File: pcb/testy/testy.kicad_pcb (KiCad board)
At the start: 2 copper layers, 114.5 x 101.4 mm, 94 parts, among them P1 OLED, P2 ICSP, SW0:0 SW_Push, SW0:1 SW_Push, SW0:2 SW_Push, SW0:3 SW_Push, SW0:4 SW_Push, SW1:0 SW_Push, SW1:1 SW_Push, SW1:2 SW_Push, SW1:3 SW_Push, SW1:4 SW_Push, SW2:0 SW_Push, SW2:1 SW_Push, SW2:2 SW_Push, SW2:3 SW_Push, SW2:4 SW_Push, SW3:0 SW_Push, SW3:1 SW_Push, SW3:2 SW_Push, SW3:3 SW_Push, SW3:4 SW_Push, SW3:5 SW_Push, SW4:1 SW_Push, SW4:2 SW_Push, SW4:3 SW_Push, SW4:4 SW_Push, SW4:5 SW_Push

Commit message: fix: undo some wrong decisions with the LEDs
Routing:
- net VCC: track 85.1 -> 61.1 mm, vias 3 -> 2
- net GND: track 238.3 -> 223.2 mm
- net LED: track 71.8 -> 57.4 mm, vias 3 -> 0
- net Net-(LED1-Pad1): track 9.55 -> 0.00 mm, vias 1 -> 0
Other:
- board text added: "TODO add extra data pin so we can handwire LEDs over the TRRS cable"
- board text added: "TODO don't directly connect the halves on the connector"
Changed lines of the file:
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@@
   (general
     (thickness 1.6)
-    (drawings 1027)
-    (tracks 1410)
+    (drawings 1029)
+    (tracks 1372)
     (zones 0)
     (modules 94)
@@
     (pad 1 thru_hole circle (at 1.166726 -1.166726 270) (size 0.7 0.7) (drill 0.4) (layers *.Cu *.Mask))
   )
+  (gr_text "TODO add extra data pin so we can\nhandwire LEDs over the TRRS cable" (at 201.83 107.7) (layer Dwgs.User)
+    (effects (font (size 1 1) (thickness 0.15)))
+  )
+  (gr_text "TODO don't directly connect the halves on the connector" (at 209.74 103.79) (layer Dwgs.User)
+    (effects (font (size 1 1) (thickness 0.15)))
+  )
   (gr_text "OLED I2C resistors" (at 170.4 90.3 90) (layer F.SilkS)
     (effects (font (size 1 1) (thickness 0.15)))
@@
   (segment (start 181.51 80.97212) (end 182.16106 80.32106) (width 0.25) (layer F.Cu) (net 5))
   (segment (start 181.51 81.53962) (end 181.51 80.97212) (width 0.25) (layer F.Cu) (net 5))
-  (segment (start 184.12 104.99) (end 184.12 98.79) (width 0.25) (layer B.Cu) (net 5))
   (segment (start 184.12 105.99) (end 184.12 104.99) (width 0.25) (layer B.Cu) (net 5))
   (segment (start 179.04 98.79) (end 179.04 97.79) (width 0.25) (layer F.Cu) (net 5))
-  (segment (start 178.79 98.79) (end 179.04 98.79) (width 0.25) (layer F.Cu) (net 5))
-  (segment (start 177.244999 100.335001) (end 178.79 98.79) (width 0.25) (layer F.Cu) (net 5))
-  (segment (start 177.244999 101.238001) (end 177.244999 100.335001) (width 0.25) (layer F.Cu) (net 5))
-  (segment (start 179.04 103.033002) (end 177.244999 101.238001) (width 0.25) (layer F.Cu) (net 5))
-  (segment (start 179.04 105.99) (end 179.04 103.033002) (width 0.25) (layer F.Cu) (net 5))
   (via (at 173.03 61.7) (size 0.8) (drill 0.4) (layers F.Cu B.Cu) (net 5))
   (segment (start 178.480001 53.349999) (end 179.33 52.5) (width 0.25) (layer F.Cu) (net 5))
@@
   (segment (start 178.96 80.97212) (end 178.35394 80.36606) (width 0.25) (layer F.Cu) (net 8))
   (segment (start 178.35394 80.36606) (end 175.45 77.46212) (width 0.25) (layer F.Cu) (net 8))
-  (segment (start 179.04 105.99) (end 179.04 98.79) (width 0.25) (layer B.Cu) (net 8))
-  (via (at 181.4 102.04) (size 0.8) (drill 0.4) (layers F.Cu B.Cu) (net 8))
-  (segment (start 181.4 101.26) (end 181.4 102.04) (width 0.25) (layer F.Cu) (net 8))
-  (segment (start 184.12 98.79) (end 183.87 98.79) (width 0.25) (layer F.Cu) (net 8))
-  (segment (start 183.87 98.79) (end 181.4 101.26) (width 0.25) (layer F.Cu) (net 8))
-  (segment (start 179.29 105.99) (end 179.04 105.99) (width 0.25) (layer B.Cu) (net 8))
-  (segment (start 181.4 103.88) (end 179.29 105.99) (width 0.25) (layer B.Cu) (net 8))
-  (segment (start 181.4 102.04) (end 181.4 103.88) (width 0.25) (layer B.Cu) (net 8))
-  (segment (start 184.12 105.99) (end 184.12 98.79) (width 0.25) (layer F.Cu) (net 8))
   (segment (start 176.55 96.55) (end 176.52 96.55) (width 0.25) (layer B.Cu) (net 8))
   (segment (start 178.79 98.79) (end 176.55 96.55) (width 0.25) (layer B.Cu) (net 8))
@@
   (segment (start 176.52 88.305218) (end 177.946499 86.878719) (width 0.25) (layer F.Cu) (net 8))
   (segment (start 176.52 90.6) (end 176.52 88.305218) (width 0.25) (layer F.Cu) (net 8))
-  (segment (start 175.02 94.8) (end 175.02 92.35) (width 0.25) (layer F.Cu) (net 9))
+  (segment (start 175.02 92.35) (end 175.02 94.8) (width 0.25) (layer B.Cu) (net 9))
   (segment (start 93.17 83.145) (end 93.175 83.15) (width 0.25) (layer F.Cu) (net 10))
   (segment (start 93.175 83.15) (end 108.1 83.15) (width 0.25) (layer F.Cu) (net 10))
@@
   (segment (start 180.84 79.07) (end 180.84 78.504315) (width 0.25) (layer F.Cu) (net 45))
   (segment (start 180.84 78.504315) (end 178.84135 76.505665) (width 0.25) (layer F.Cu) (net 45))
-  (segment (start 180.54 100.83) (end 180.17 100.83) (width 0.25) (layer B.Cu) (net 46))
-  (via (at 180.17 100.83) (size 0.8) (drill 0.4) (layers F.Cu B.Cu) (net 46))
-  (segment (start 181.58 98.79) (end 181.58 99.79) (width 0.25) (layer B.Cu) (net 46))
-  (segment (start 181.58 99.79) (end 180.54 100.83) (width 0.25) (layer B.Cu) (net 46))
-  (segment (start 181.33 105.99) (end 181.58 105.99) (width 0.25) (layer F.Cu) (net 46))
-  (segment (start 180.17 104.83) (end 181.33 105.99) (width 0.25) (layer F.Cu) (net 46))
-  (segment (start 180.17 100.83) (end 180.17 104.83) (width 0.25) (layer F.Cu) (net 46))
-  (via (at 177.97 100.89) (size 0.8) (drill 0.4) (layers F.Cu B.Cu) (net 46))
-  (segment (start 180.17 100.83) (end 178.03 100.83) (width 0.25) (layer F.Cu) (net 46))
-  (segment (start 178.03 100.83) (end 177.97 100.89) (width 0.25) (layer F.Cu) (net 46))
-  (segment (start 177.404315 100.89) (end 175.43 98.915685) (width 0.25) (layer B.Cu) (net 46))
-  (segment (start 177.97 100.89) (end 177.404315 100.89) (width 0.25) (layer B.Cu) (net 46))
-  (via (at 175.43 98.915685) (size 0.8) (drill 0.4) (layers F.Cu B.Cu) (net 46))
   (segment (start 184.403701 52.510299) (end 185.28 51.634) (width 0.25) (layer F.Cu) (net 46))
   (segment (start 184.078699 52.835301) (end 184.403701 52.510299) (width 0.25) (layer F.Cu) (net 46))
@@
   (segment (start 173.89 82.54038) (end 173.9 82.53038) (width 0.25) (layer B.Cu) (net 50))
   (segment (start 173.89 84.88) (end 173.89 82.54038) (width 0.25) (layer B.Cu) (net 50))
-  (via (at 182.58 102.98) (size 0.8) (drill 0.4) (layers F.Cu B.Cu) (net 54))
-  (segment (start 181.58 98.79) (end 181.58 99.79) (width 0.25) (layer F.Cu) (net 54))
-  (segment (start 181.266998 102.98) (end 182.58 102.98) (width 0.25) (layer F.Cu) (net 54))
-  (segment (start 181.58 99.79) (end 180.94999 100.42001) (width 0.25) (layer F.Cu) (net 54))
-  (segment (start 180.94999 100.42001) (end 180.94999 101.417008) (width 0.25) (layer F.Cu) (net 54))
-  (segment (start 180.674999 102.388001) (end 181.266998 102.98) (width 0.25) (layer F.Cu) (net 54))
-  (segment (start 180.674999 101.691999) (end 180.674999 102.388001) (width 0.25) (layer F.Cu) (net 54))
-  (segment (start 180.94999 101.417008) (end 180.674999 101.691999) (width 0.25) (layer F.Cu) (net 54))
-  (segment (start 182.58 104.99) (end 181.58 105.99) (width 0.25) (layer B.Cu) (net 54))
-  (segment (start 182.58 102.98) (end 182.58 104.99) (width 0.25) (layer B.Cu) (net 54))
   (zone (net 0) (net_name "") (layer B.Cu) (hatch edge 0.508)
     (connect_pads (clearance 0.508))

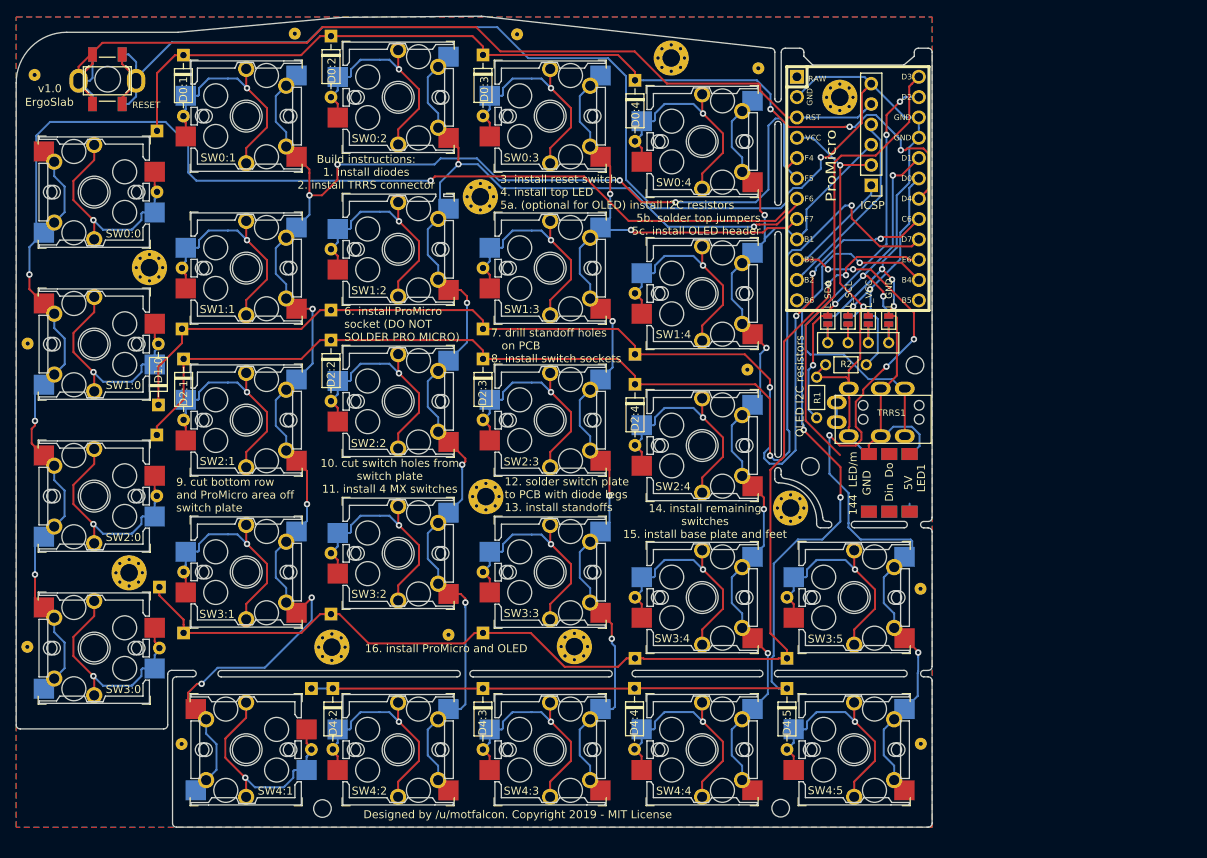
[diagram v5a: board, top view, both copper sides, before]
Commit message: fix: correct (I think) the LED wiring
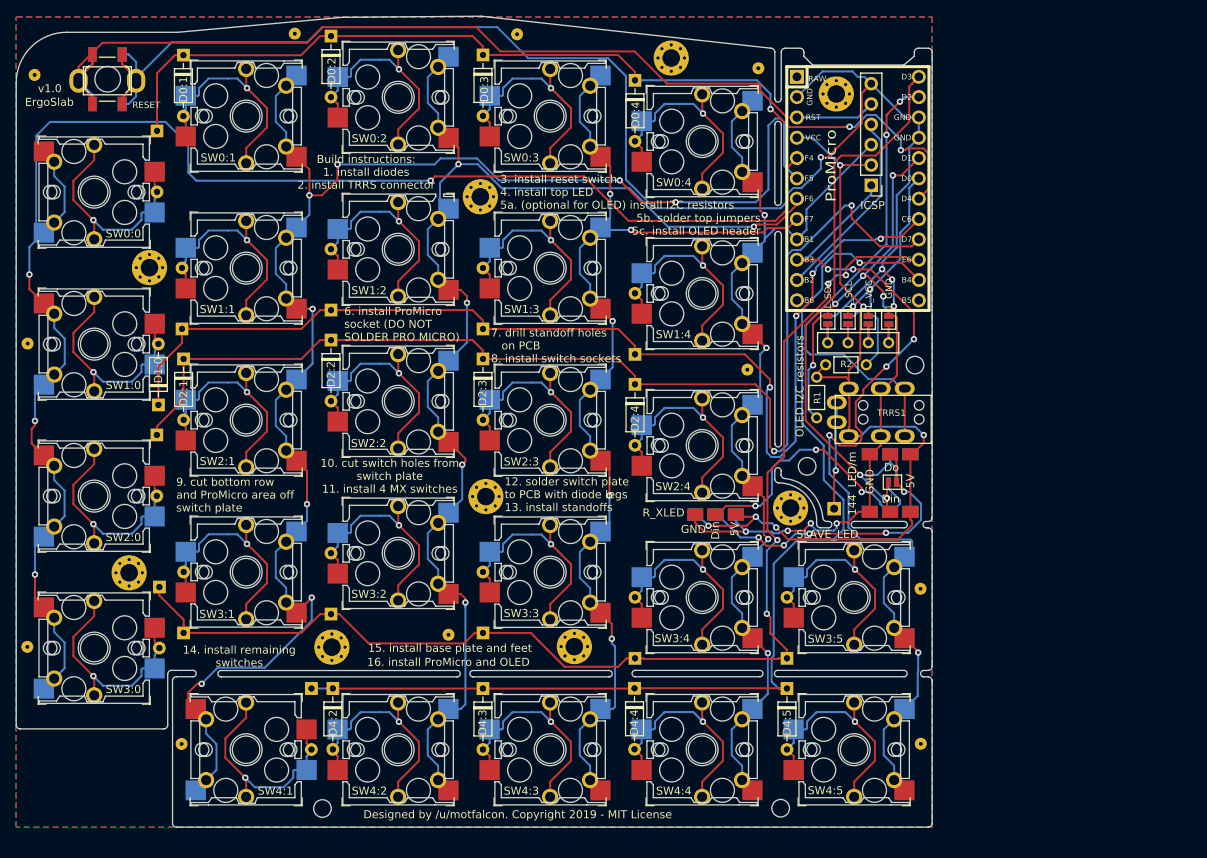
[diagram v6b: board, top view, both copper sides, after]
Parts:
- removed LED1: SK6812mini, footprints:ws2812-single
- added J1: L_XLED, footprints:ws2812-strip, B.Cu at (160.1, 106.0)
- added J2: R_XLED, footprints:ws2812-strip, F.Cu at (159.7, 106.0)
- added J3: SLAVE_LED, footprints:PinHeader_1x01_P2.54mm_Vertical, F.Cu at (174.7, 105.6)
- added JP12: R_NOLED, footprints:Jumper, B.Cu at (182.0, 102.3)
- added JP9: L_NOLED, footprints:Jumper, F.Cu at (182.0, 102.3)
- added LED_L1: SK6812mini, footprints:ws2812-single, F.Cu at (181.5, 102.2)
- added LED_R1: SK6812mini, footprints:ws2812-single, B.Cu at (181.5, 102.6)
- moved Drill 0.61 mm to (175.0, 53.8)
- moved HOLE_M2 0.40 mm to (171.3, 100.3)
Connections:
- net Col6 renamed MOSI
- TRRS1 pad 1: Net-(TRRS1-Pad1) -> SLAVE_LED
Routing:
- net VCC: track 61.1 -> 112.9 mm, vias 2 -> 6
- net Net-(J1-Pad2): track 0.00 -> 38.9 mm, vias 0 -> 5
- net Net-(J2-Pad2): track 0.00 -> 35.7 mm, vias 0 -> 3
- net GND: track 223.2 -> 249.4 mm, vias 4 -> 8
- net LED: track 57.4 -> 77.7 mm, vias 0 -> 2
- net SLAVE_LED: track 0.00 -> 13.4 mm, vias 0 -> 1
- net Net-(TRRS1-Pad1): track 2.45 -> 0.00 mm
- net Row2: track 146.7 -> 144.3 mm
- net Row1: track 144.3 -> 142.1 mm
- net Row3: track 151.8 -> 153.2 mm, vias 2 -> 4
- net Row4: track 136.4 -> 137.5 mm, vias 3 -> 1
- net Reset: track 124.8 -> 124.0 mm
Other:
- outline, holes or cut-outs redrawn
- board text added: "14. install remaining switches"
- board text added: "15. install base plate and feet"
- board text removed: "14. install remaining switches 15. install base plate and feet"

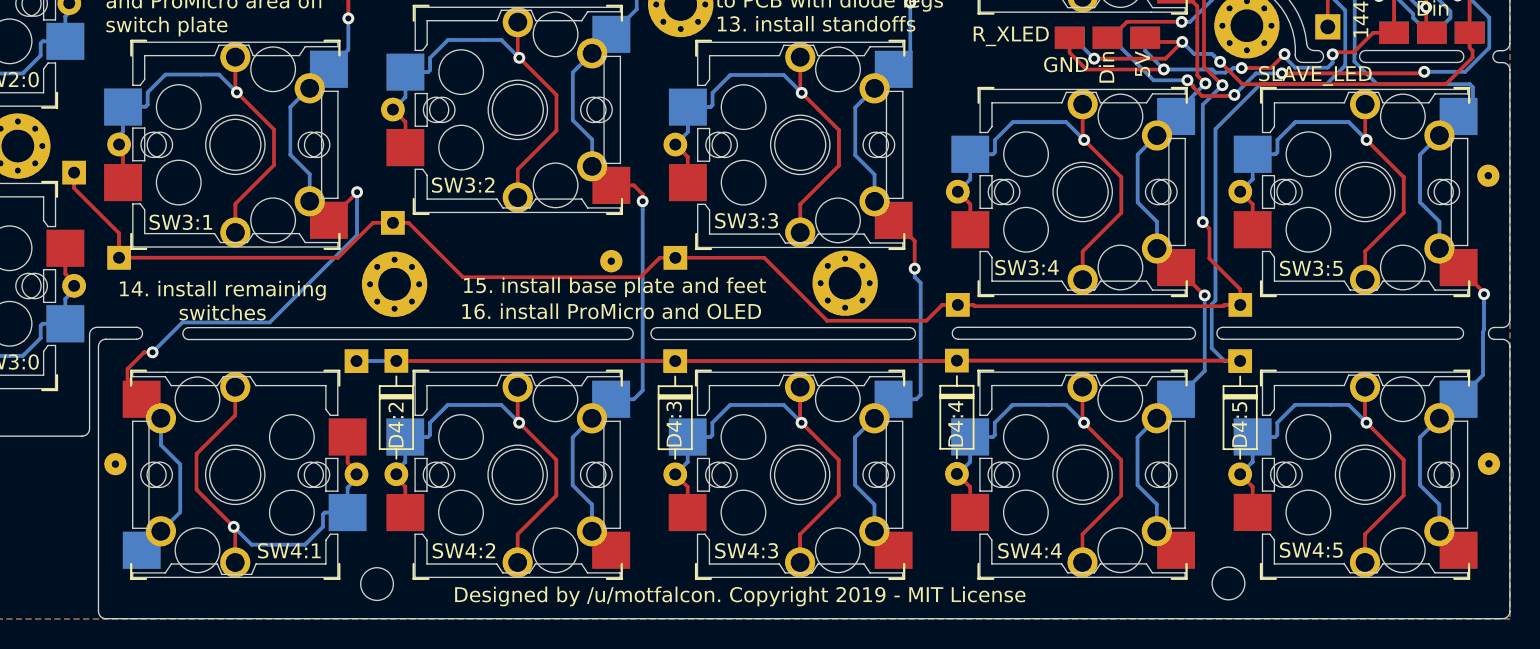
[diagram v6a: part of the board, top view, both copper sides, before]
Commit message: feat: create a choc-only footprint and use that for the bottom row, check that making the other switches MX only will remove DRC errors and it will, so that needs to be done. Also add choc reference PDF
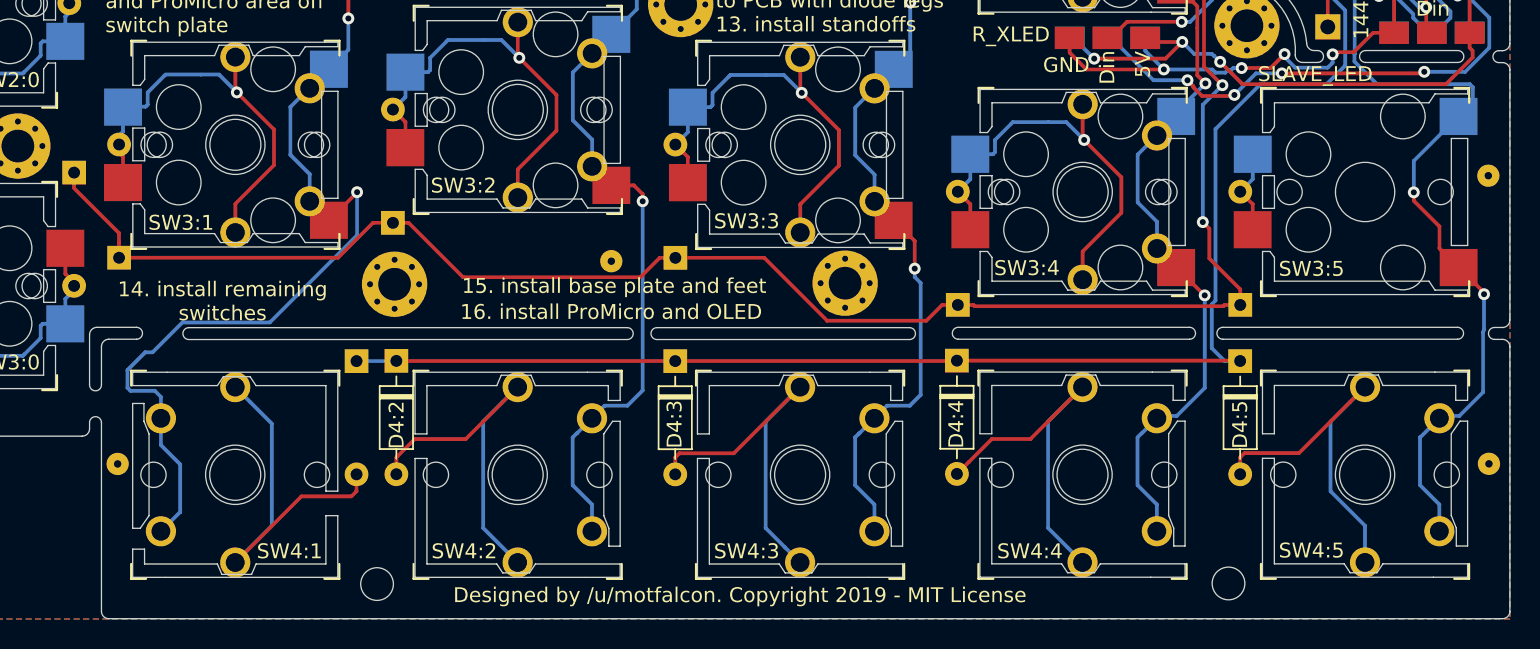
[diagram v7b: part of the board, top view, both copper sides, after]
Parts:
- SW3:5: footprint footprints:kailh-socket-and-choc-solder-reversible -> footprints:Kailh_socket_reversible
- moved REF** 0.15 mm to (93.3, 135.0)
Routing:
- net Net-(D3:5-Pad2): track 29.1 -> 5.78 mm, vias 1 -> 0
- net Net-(D4:4-Pad2): track 29.1 -> 24.6 mm, vias 1 -> 0
- net Net-(D4:2-Pad2): track 29.1 -> 25.0 mm, vias 1 -> 0
- net Net-(D4:1-Pad2): track 29.1 -> 25.1 mm, vias 1 -> 0
- net Net-(D4:5-Pad2): track 29.1 -> 25.2 mm, vias 1 -> 0
- net Net-(D4:3-Pad2): track 29.1 -> 25.2 mm, vias 1 -> 0
- net Col3: track 131.3 -> 129.5 mm
- net Col2: track 160.9 -> 159.1 mm
- net Col1: track 203.1 -> 201.3 mm, vias 8 -> 7
- net Col4: track 124.1 -> 122.9 mm
- net Col5: track 113.7 -> 112.9 mm, vias 6 -> 7
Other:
- outline, holes or cut-outs redrawn
- board text removed: "TODO add WSxxxx LED solder on points with jumpers to bypass"
- board text removed: "TODO add extra data pin so we can handwire LEDs over the TRRS cable"
- board text removed: "TODO don't directly connect the halves on the connector"
